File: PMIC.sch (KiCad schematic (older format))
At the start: 63 parts, among them J1001 TEST_1P, U1001 PF3000

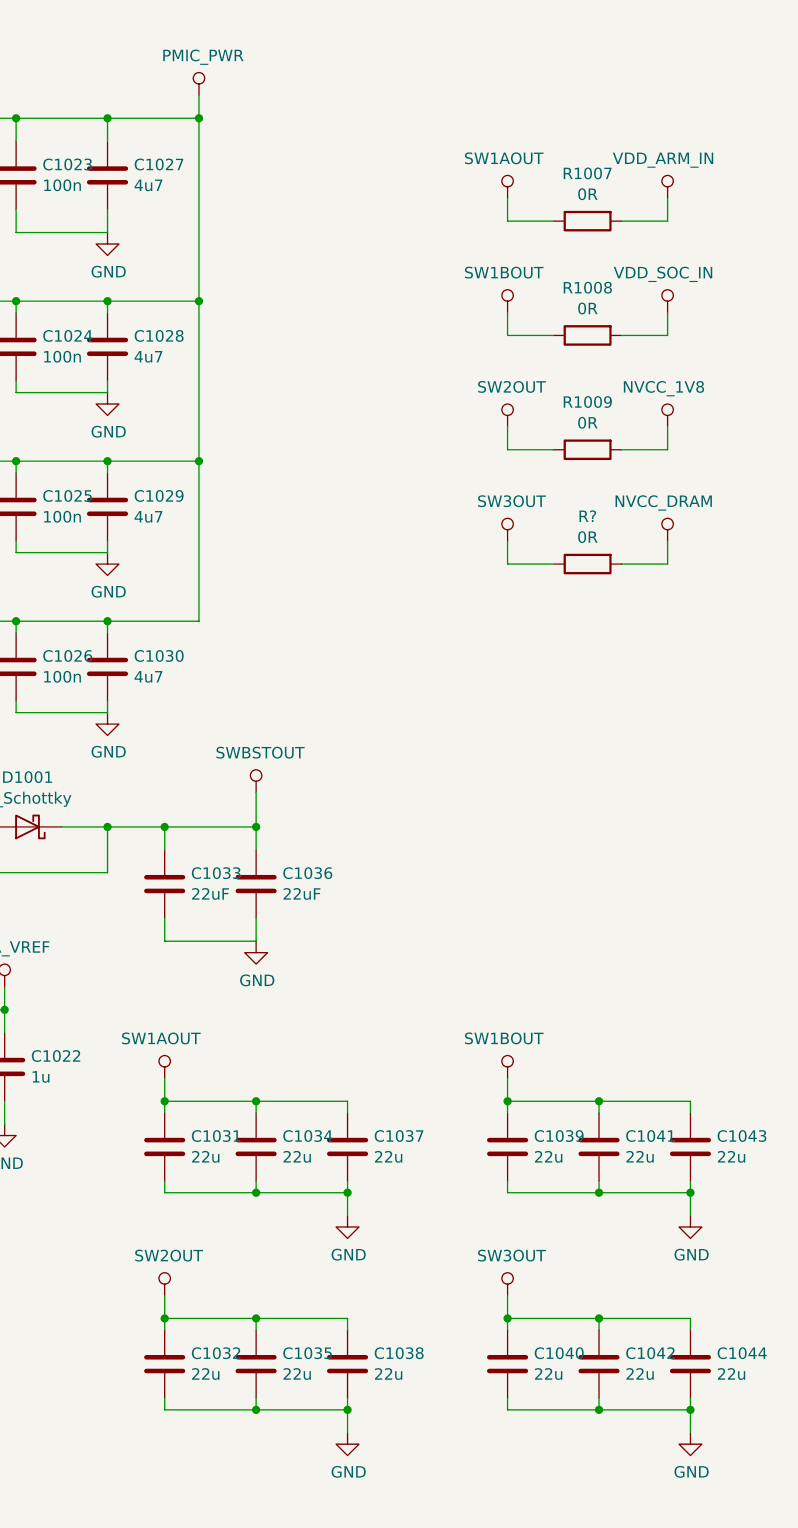
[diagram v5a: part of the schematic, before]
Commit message: Changed several voltage rail connections Removed non existing rails Added circuit for NiMH charging
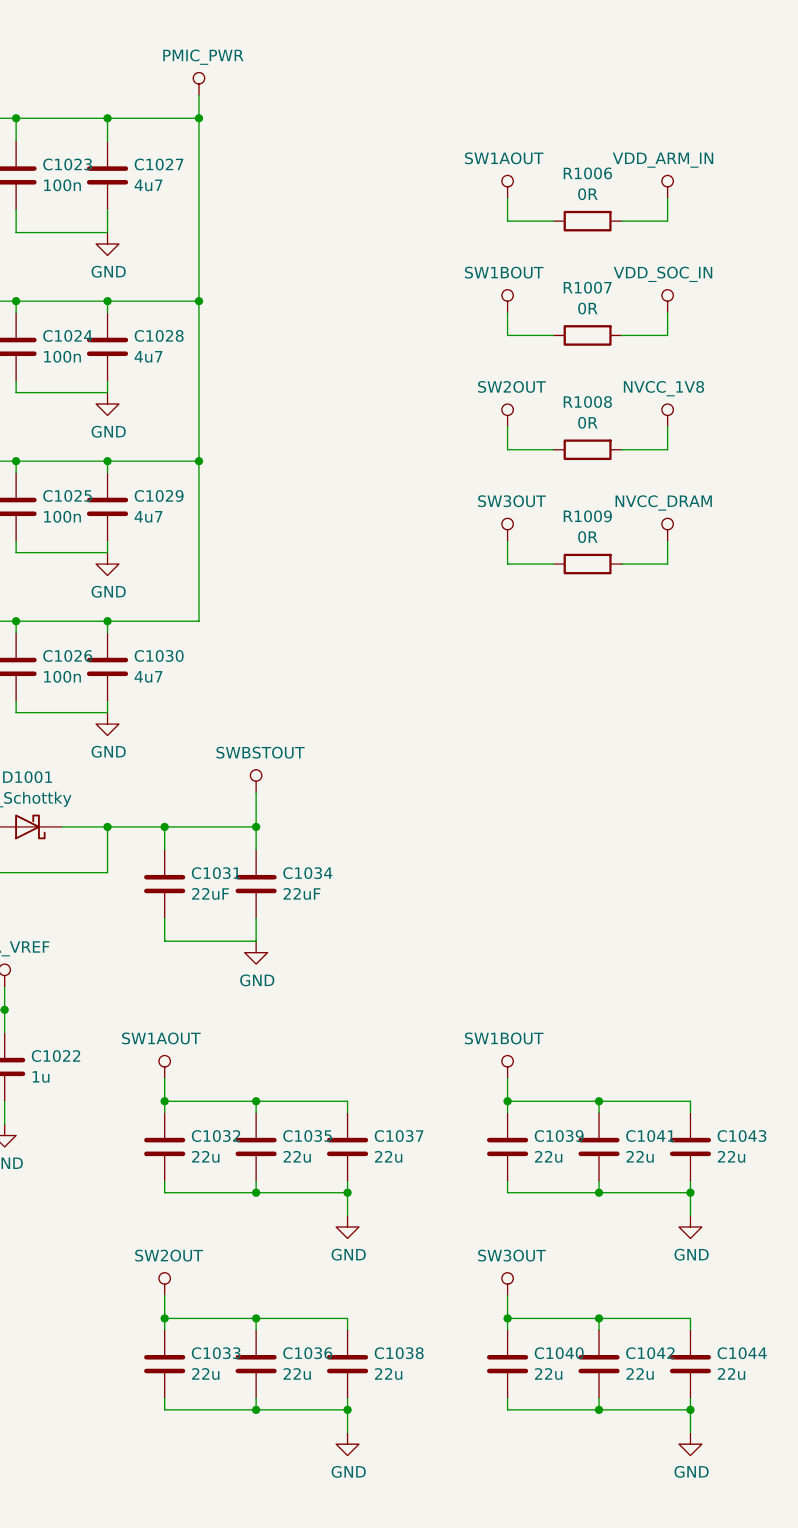
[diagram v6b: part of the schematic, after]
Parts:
- gave numbers to parts that had none: 1
- renumbered C1033 to C1031, C1031 to C1032, C1032 to C1033, C1036 to C1034, C1034 to C1035, C1035 to C1036, R1007 to R1006, R1008 to R1007, R1009 to R1008

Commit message: Created netlist with current components Foreward Annotation to Board
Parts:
- BT1001: footprint (none) -> Pin_Headers:Pin_Header_Straight_1x02
- C1001, C1002, C1003, C1004, C1005, C1006, C1007, C1008, C1010, C1011, C1012, C1013, C1015, C1018, C1022, C1027, C1028, C1029, C1030, C1031, C1032, C1033, C1034, C1035, C1036, C1037, C1038, C1039, C1040, C1041, C1042, C1043, C1044: footprint (none) -> Capacitors_SMD:C_0603
- C1009, C1014, C1016, C1017, C1019, C1020, C1021, C1023, C1024, C1025, C1026: footprint (none) -> Capacitors_SMD:C_0402
- D1001: footprint (none) -> Diodes_SMD:DD-PAK_TO263_SingleDiode
- J1001: footprint (none) -> NokiaRetroFit:TP
- L1001: footprint Resistors_SMD:R_0603 -> Choke_SMD:Choke_SMD_1206_Standard
- L1002, L1003, L1004, L1005, L1006: footprint (none) -> Choke_SMD:Choke_SMD_1206_Standard
- R1001, R1002, R1003, R1004, R1005, R1006, R1007, R1008, R1009: footprint (none) -> Resistors_SMD:R_0402
- U1001: footprint (none) -> Housings_DFN_QFN:QFN-48-1EP_7x7mm_Pitch0.5mm
